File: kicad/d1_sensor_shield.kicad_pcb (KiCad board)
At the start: 2 copper layers, 26.9 x 35.6 mm, 14 parts, among them U1 WeMos_D1_mini, U2 LM75B, U3 W25Q16JV

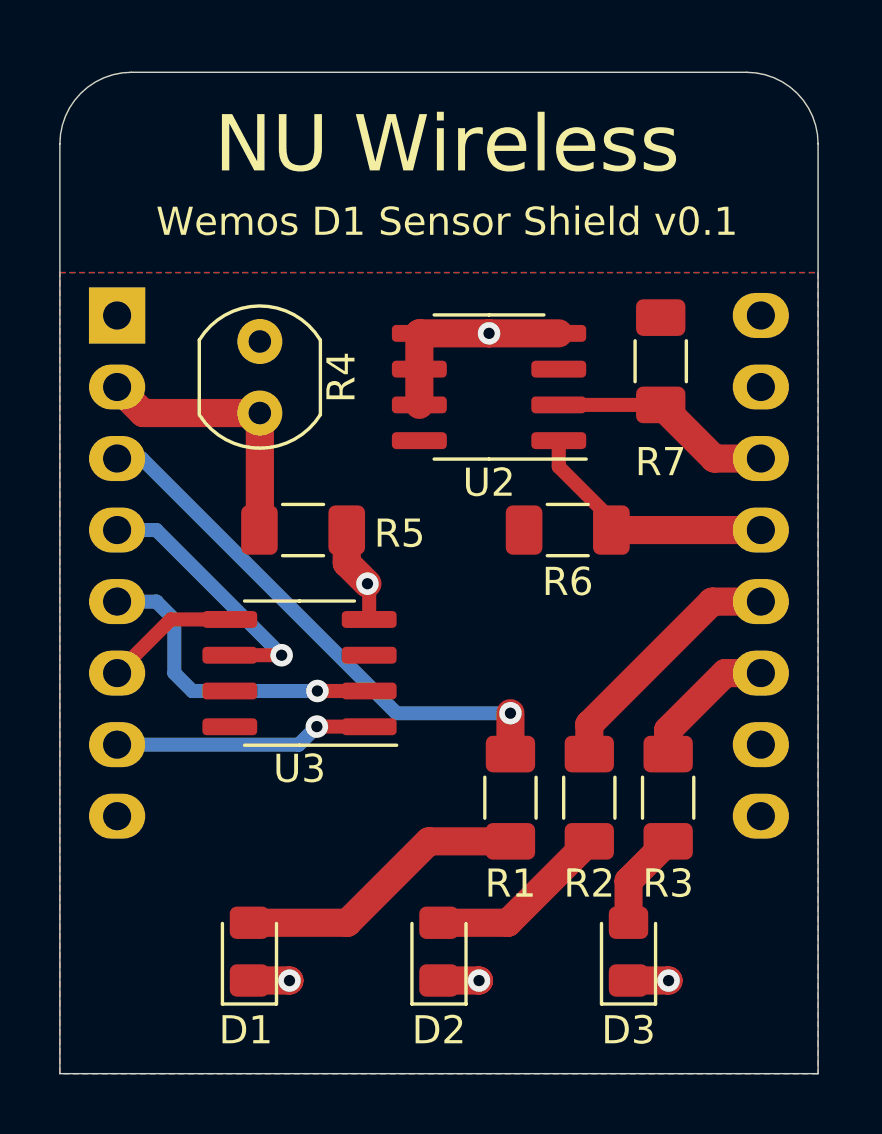
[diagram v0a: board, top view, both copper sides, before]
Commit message: Flip D1 to other side of board
Wemos D1 footprint was incorrectly placed
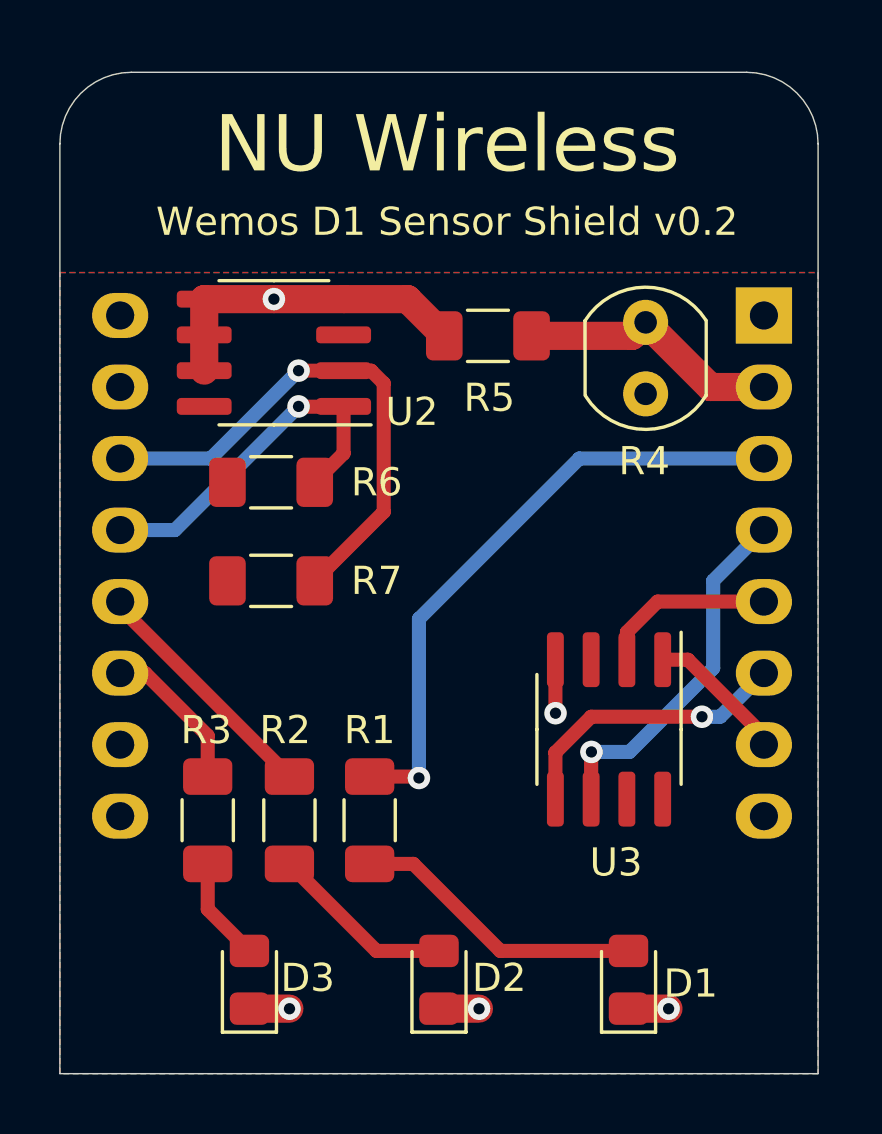
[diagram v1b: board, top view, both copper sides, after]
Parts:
- U1: moved to B.Cu
- moved U1 23.0 mm to (79.4, 55.9), turned to 180 degrees
- moved R3 16.4 mm to (59.6, 73.8)
- moved R7 15.9 mm to (61.9, 65.3), turned to 0 degrees
- moved R4 13.8 mm to (75.2, 58.7), turned to 90 degrees
- moved D1 13.5 mm to (74.5, 79.5)
- moved D3 13.5 mm to (61.1, 79.5)
- moved U3 11.2 mm to (73.9, 70.6), turned to -90 degrees
- moved R2 10.7 mm to (62.5, 73.8)
- moved R6 10.7 mm to (61.9, 61.8)
- moved R5 9.52 mm to (69.6, 56.6), turned to 180 degrees
- moved U2 7.74 mm to (62.0, 57.2)
- moved R1 5.06 mm to (65.4, 73.8)
- moved D2 1.00 mm to (67.8, 79.5)
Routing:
- net SCL: track 8.15 -> 18.9 mm, vias 0 -> 1
- net MOSI: track 4.79 -> 10.2 mm, vias 0 -> 1
- net MISO: track 11.4 -> 6.45 mm, vias 1 -> 0
- net CS: track 9.22 -> 5.03 mm, vias 1 -> 0
- net SDA: track 9.26 -> 12.9 mm, vias 0 -> 1
- net SCK: track 9.52 -> 12.9 mm
- net LED1: track 19.2 -> 22.0 mm
- net GND: track 15.3 -> 17.8 mm
- net LED3: track 4.98 -> 5.48 mm
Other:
- board text added: "3V3"
- board text added: "5V"
- board text added: "A0"
- board text added: "D0"
- board text added: "D1"
- board text added: "D2"
- board text added: "D3"
- board text added: "D4"
- board text added: "D5"
- board text added: "D6"
- board text added: "D7"
- board text added: "D8"
- board text added: "GND"
- board text added: "RST"
- board text added: "RX"
- board text added: "TX"
- board text added: "Wemos D1 Sensor Shield v0.2"
- board text removed: "Wemos D1 Sensor Shield v0.1"

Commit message: Redo edge cuts in 10mil thickness, move silkscreen
also shift oshw logo
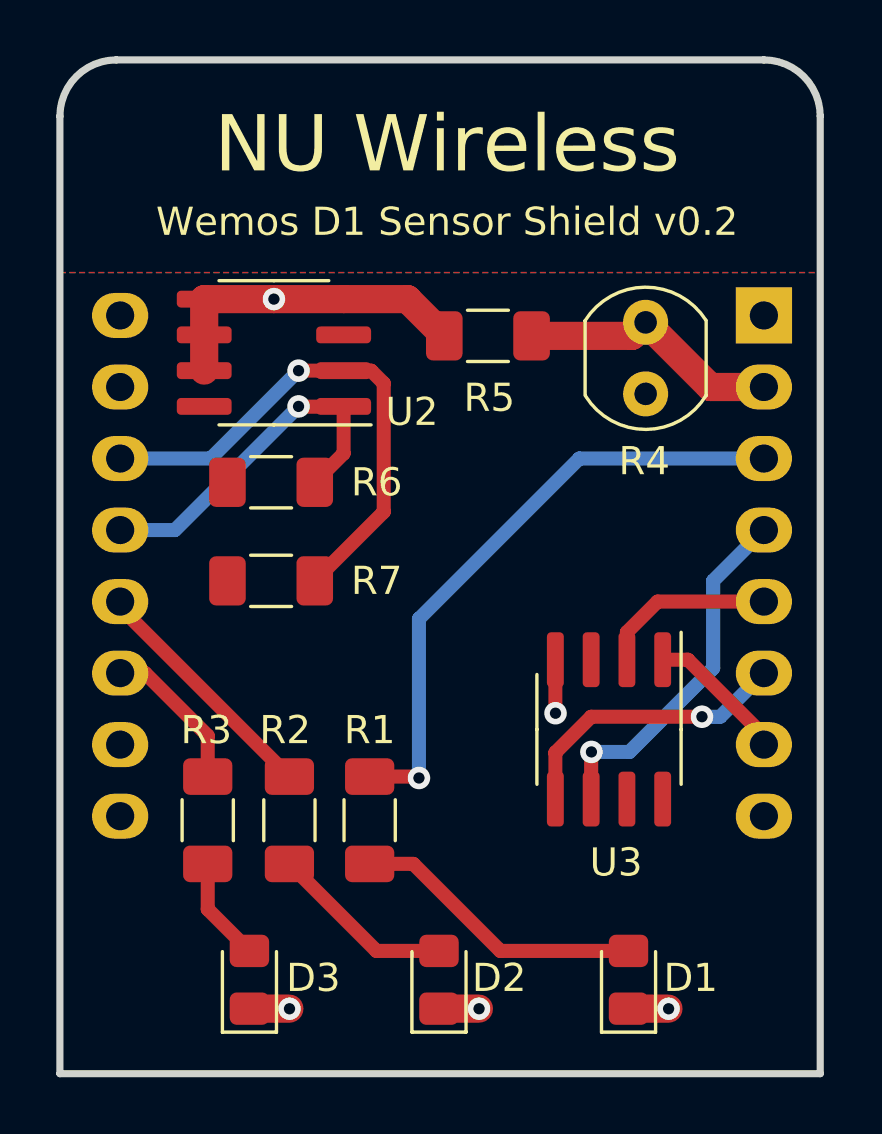
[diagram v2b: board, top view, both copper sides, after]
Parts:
- moved REF** 18.4 mm to (58.1, 79.8), turned to 0 degrees
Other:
- board size 26.9 x 35.6 mm -> 27 x 36 mm

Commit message: Update SPI flash footprint, silkscreen
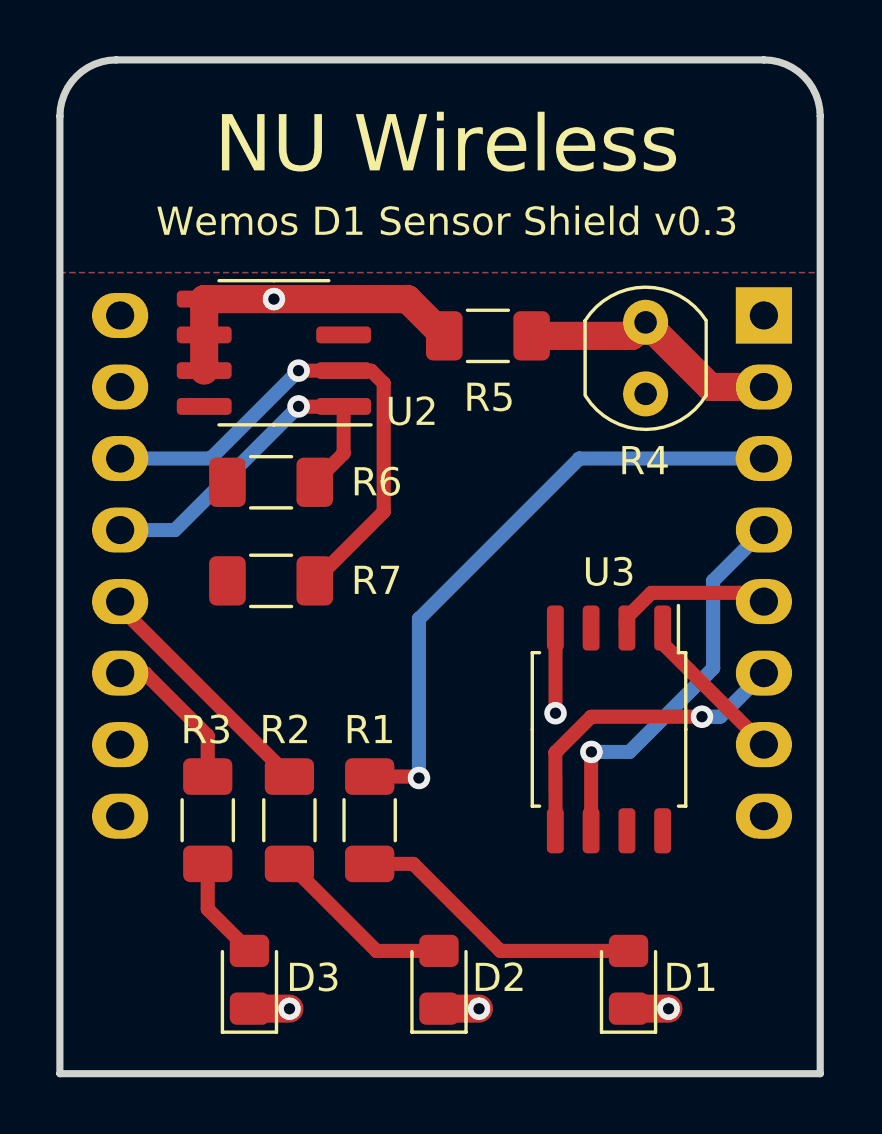
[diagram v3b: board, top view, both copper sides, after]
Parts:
- removed the REF** at (58.1, 79.8)
- added REF**: OSHW-Logo2_7.3x6mm_SilkScreen, Symbol:OSHW-Logo2_7.3x6mm_SilkScreen, F.Cu at (57.9, 79.8)
- U3: footprint Package_SO:SOIC-8_3.9x4.9mm_P1.27mm -> Package_SO:SOIC-8_5.23x5.23mm_P1.27mm
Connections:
- U1 pad 1: no_connect_16 -> (no net)
- U1 pad 15: no_connect_17 -> (no net)
- U1 pad 16: no_connect_18 -> (no net)
- U1 pad 9: no_connect_19 -> (no net)
- U2 pad 3: no_connect_20 -> (no net)
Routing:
- net MOSI: track 10.2 -> 11.4 mm
- net SCK: track 12.9 -> 14.0 mm
- net GND: track 17.8 -> 18.9 mm
- net MISO: track 6.45 -> 5.76 mm
- net CS: track 5.03 -> 5.63 mm
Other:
- board text added: "JLCJLCJLCJLC"
- board text added: "Wemos D1 Sensor Shield v0.3"
- board text removed: "Wemos D1 Sensor Shield v0.2"

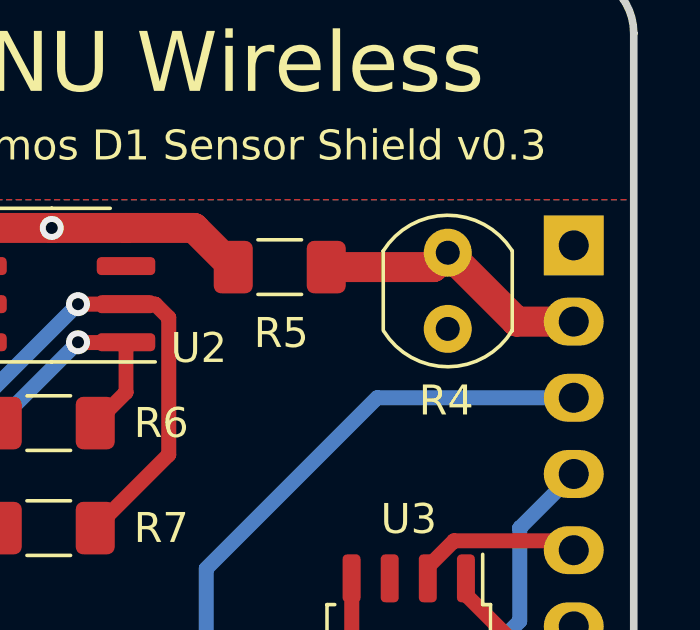
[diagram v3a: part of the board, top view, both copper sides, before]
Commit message: widen photocell footprint
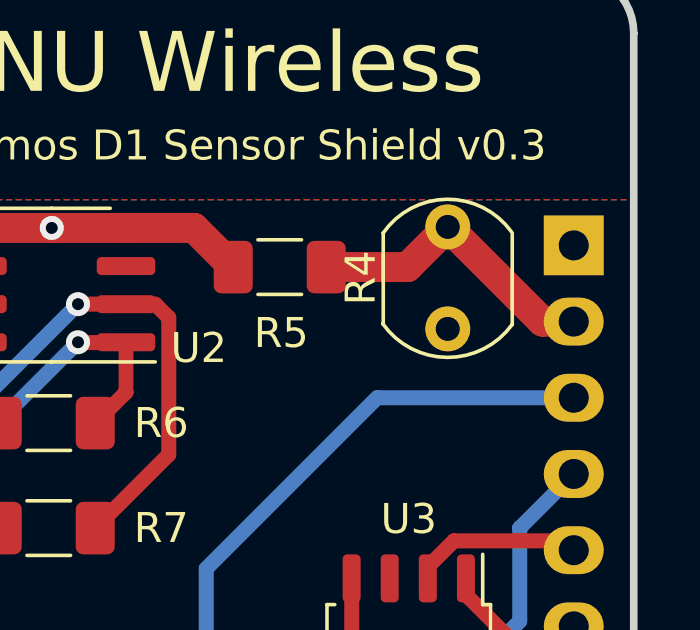
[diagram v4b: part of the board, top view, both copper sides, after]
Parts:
- removed REF**: OSHW-Logo2_7.3x6mm_SilkScreen, Symbol:OSHW-Logo2_7.3x6mm_SilkScreen
- R1, R2, R3: value 68 -> 1k5
- R4: footprint OptoDevice:R_LDR_4.9x4.2mm_P2.54mm_Vertical -> OptoDevice:R_LDR_5.1x4.3mm_P3.4mm_Vertical
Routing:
- net PHOTOCELL: track 9.40 -> 10.1 mm

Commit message: v0.4, change size slightly
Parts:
- added REF**: OSHW-Logo2_7.3x6mm_Copper, Symbol:OSHW-Logo2_7.3x6mm_Copper, F.Cu at (58.2, 79.0)
- moved D1 0.67 mm to (74.5, 78.8)
- moved D2 0.67 mm to (67.8, 78.8)
- moved D3 0.67 mm to (61.1, 78.8)
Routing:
- net Net-(D3-Pad2): track 3.73 -> 3.04 mm
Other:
- board size 27 x 36 mm -> 26 x 34 mm
- board text added: "Wemos D1 Sensor Shield v0.4"
- board text removed: "Wemos D1 Sensor Shield v0.3"
